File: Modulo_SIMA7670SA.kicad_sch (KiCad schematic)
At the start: 64 parts, among them J1 TBP01R1-508-02BE, J2 DB9 Hembra Impreso 90°, J3 U.FL IPEX1 MALE, J4 SMA-J-P-X-RA-TH1, J5 Jack DC 2.1mm PCB recto, Q1 BSS138, Q2 FDN340P, Q3 FDN340P, Q4 BSS138, Q5 BC327, Q6 2N7000, U1 MAX232, U2 24LC512, U3 BKP-A7670SA (Módulo SIMCOM), U4 MAX706, U5 Black_Pill_STM32F411CEUx, U6 LM2596S_Modulo_Regulable, U7 LM7805_TO220

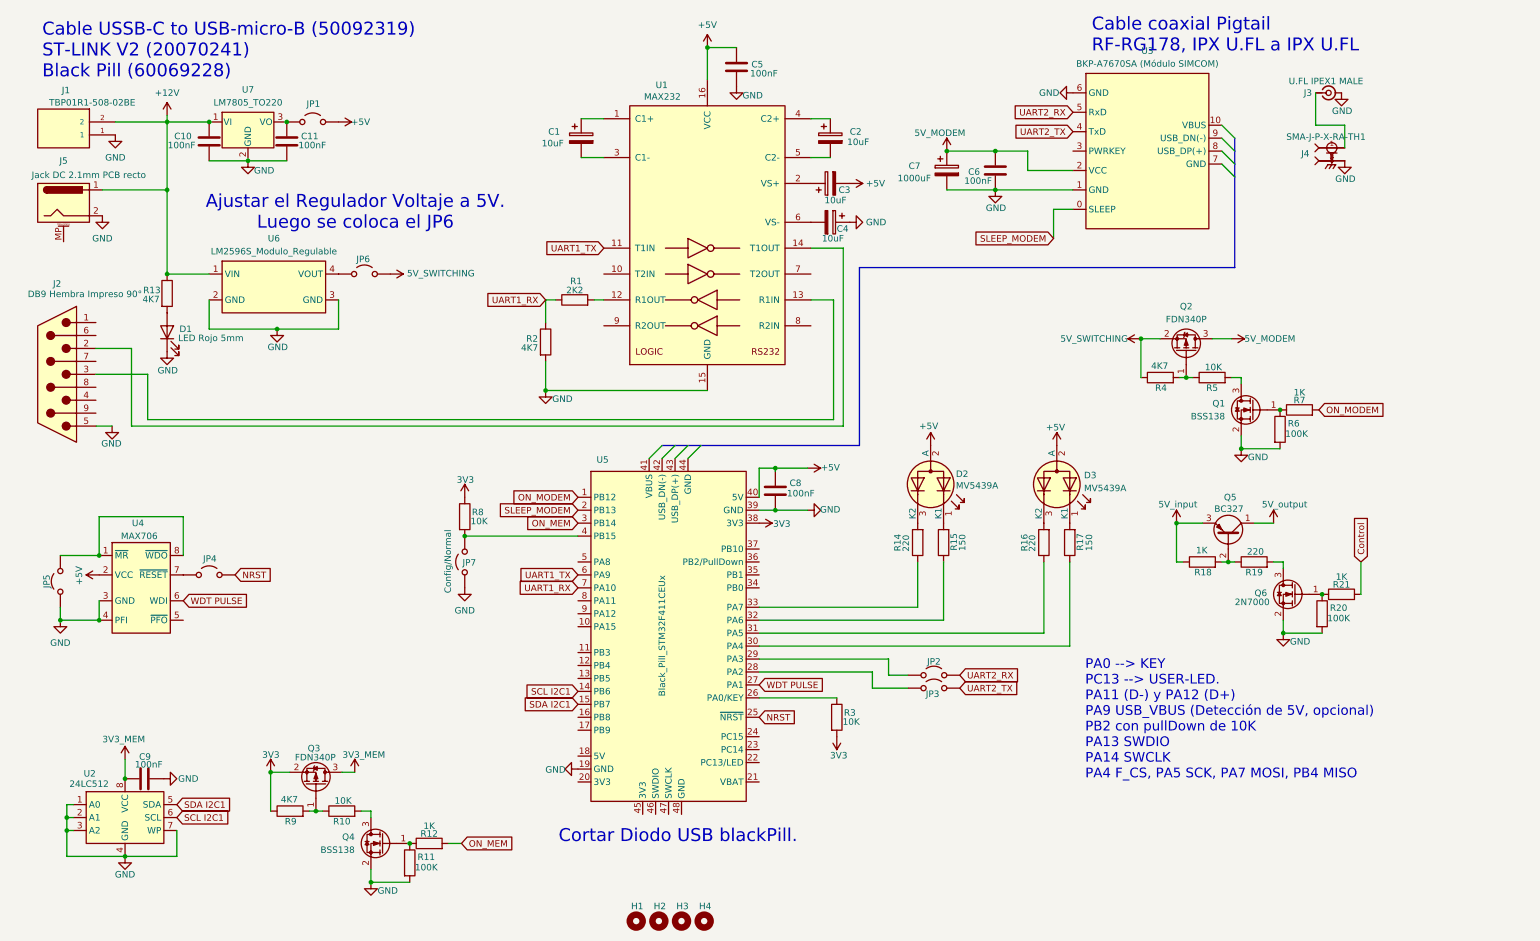
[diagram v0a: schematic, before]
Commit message: Se hicieron modificaciones en los circuitos mosfet para controlar on/off del BKP-A7670SA y de la 24C512.
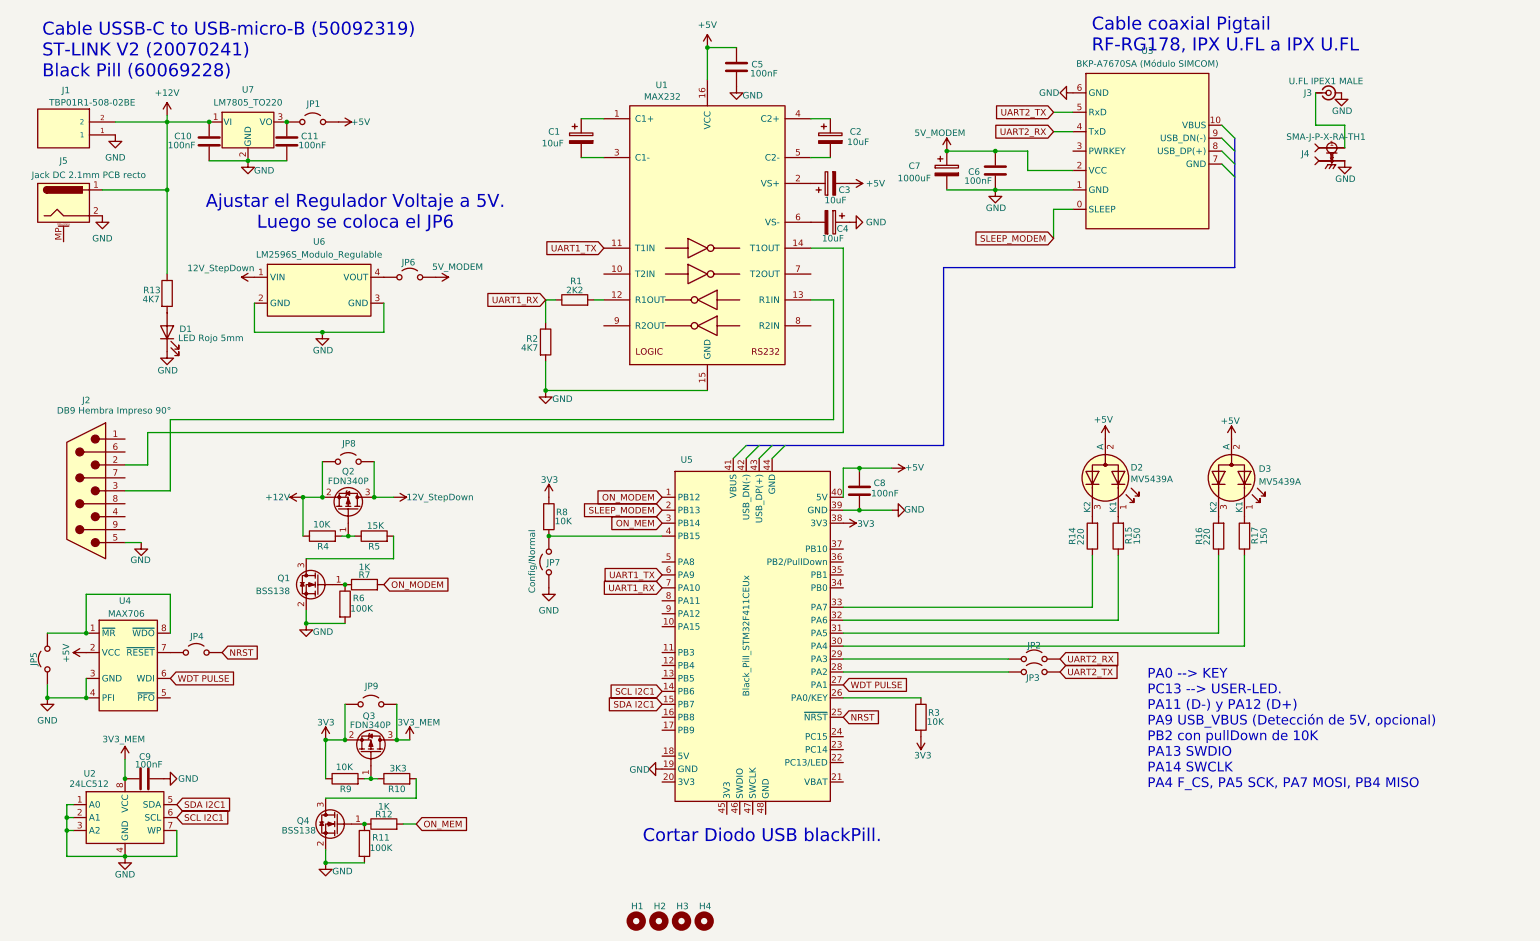
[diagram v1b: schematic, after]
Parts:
- removed Q5: BC327, Package_TO_SOT_THT:TO-92_Inline, symbol Transistor_BJT:BC327
- removed Q6: 2N7000, Package_TO_SOT_SMD:SOT-23, symbol Transistor_FET:BSS138
- removed R18, R21: 1K, Resistor_SMD:R_0805_2012Metric, symbol Device:R
- removed R19: 220, Resistor_SMD:R_0805_2012Metric, symbol Device:R
- removed R20: 100K, Resistor_SMD:R_0805_2012Metric, symbol Device:R
- added JP8, JP9: Jumper_2_Open, Connector_PinHeader_2.54mm:PinHeader_1x02_P2.54mm_Vertical, symbol Jumper:Jumper_2_Open
- R10: value 10K -> 3K3
- R4, R9: value 4K7 -> 10K
- R5: value 10K -> 15K
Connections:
- net +12V: now also Q2.2 (S), R4.1, JP8.1 (A); no longer U6.1 (VIN)
- net 3V3: now also JP9.1 (A)
- net 3V3_MEM: now also JP9.2 (B)
- net 5V_MODEM: now also JP6.2 (B); no longer Q2.3 (D)
- net UART2_RX: now also U3.4 (TxD); no longer U3.5 (RxD)
- net UART2_TX: now also U3.5 (RxD); no longer U3.4 (TxD)
- removed net 5V_SWITCHING: JP6.2 (B), Q2.2 (S), R4.1
- new net 12V_StepDown: JP8.2 (B), Q2.3 (D), U6.1 (VIN)
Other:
- moved on the sheet: C8, D2, D3, J2, JP2, JP3, JP4, JP5, JP6, JP7, Q1, Q2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

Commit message: Estamos haciendo un nuevo PCB porque se hicieron mpodificaciones en el circuito eléctrico para manejar la señal de ON/OFF del BKP-A7670SA en el riel de los 12V.
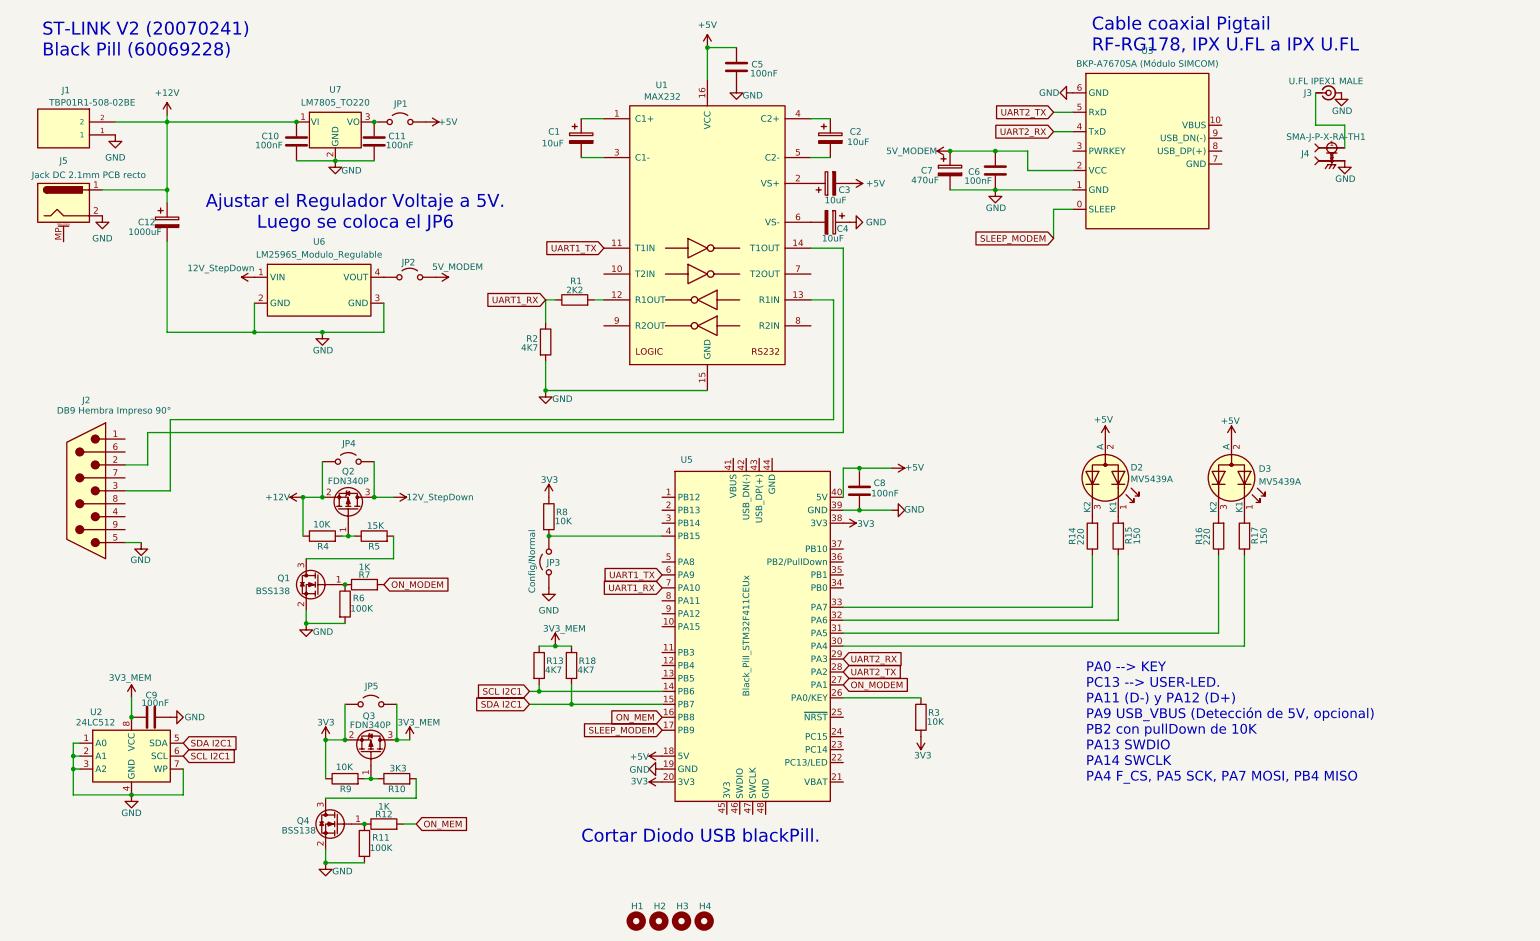
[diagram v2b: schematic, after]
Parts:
- removed D1: LED Rojo 5mm, LED_THT:LED_D5.0mm, symbol Device:LED
- removed JP2, JP3, JP4, JP5: Jumper_2_Open, Connector_PinHeader_2.54mm:PinHeader_1x02_P2.54mm_Vertical, symbol Jumper:Jumper_2_Open
- removed U4: MAX706, Package_SO:SOIC-8_3.9x4.9mm_P1.27mm, symbol New_Library:MAX705
- added C12: 1000uF, Capacitor_THT:CP_Radial_D8.0mm_P5.00mm, symbol Device:C_Polarized
- added R18: 4K7, Resistor_SMD:R_0805_2012Metric, symbol Device:R
- C7: value 1000uF -> 470uF
- renumbered JP6 to JP2, JP7 to JP3, JP8 to JP4, JP9 to JP5
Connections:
- net WDT PULSE is gone; now on net ON_MODEM: U5.27 (PA1)
- net +12V: now also C12.1; no longer R13.1
- net +5V: now also U5.18 (5V)
- net 3V3: now also U5.20 (3V3)
- net 3V3_MEM: now also R13.1, R18.1
- net GND: now also C12.2
- net ON_MEM: now also U5.16 (PB8); no longer U5.3 (PB14)
- net ON_MODEM: no longer U5.1 (PB12)
- net SCL I2C1: now also R13.2
- net SDA I2C1: now also R18.2
- net SLEEP_MODEM: now also U5.17 (PB9); no longer U5.2 (PB13)
- net UART2_RX: now also U5.29 (PA3)
- net UART2_TX: now also U5.28 (PA2)
- net NRST: no longer names the net of U5.25 (~{NRST})
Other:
- note added: "ST-LINK V2 (20070241) Black Pill (60069228)"
- note removed: "Cable USSB-C to USB-micro-B (50092319) ST-LINK V2 (20070241) Black Pill (60069228)"
- moved on the sheet: C10, C11, C9, JP1, U2, U7

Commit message: Adelantando algo del PCB. Fue ncesario modificar GPIOs del STM32 y renombrar rieles de 3.3V; 5V; y GND, para que no tengamos líneas sin rutear.
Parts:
- added C13: 470uF, Capacitor_THT:CP_Radial_D8.0mm_P5.00mm, symbol Device:C_Polarized
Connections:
- net +5V: now also C13.1
- net 3V3: no longer JP5.1 (A), Q3.2 (S), R9.1, U5.20 (3V3)
- net GND: now also C13.2
- new net 3V3_b: JP5.1 (A), Q3.2 (S), R9.1, U5.20 (3V3)
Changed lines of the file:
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@@
 	)
 	(junction
+		(at 186.69 102.87)
+		(diameter 0)
+		(color 0 0 0 0)
+	)
+	(junction
 		(at 119.38 148.59)
 		(diameter 0)
@@
 	)
 	(junction
-		(at 175.895 110.49)
+		(at 114.935 115.57)
 		(diameter 0)
 		(color 0 0 0 0)
 	)
 	(junction
-		(at 114.935 115.57)
+		(at 71.12 179.705)
 		(diameter 0)
 		(color 0 0 0 0)
 	)
 	(junction
-		(at 71.12 179.705)
+		(at 40.005 47.625)
 		(diameter 0)
 		(color 0 0 0 0)
 	)
 	(junction
-		(at 40.005 47.625)
+		(at 175.895 102.87)
 		(diameter 0)
 		(color 0 0 0 0)
@@
 	)
 	(junction
-		(at 175.895 102.235)
+		(at 71.12 155.575)
 		(diameter 0)
 		(color 0 0 0 0)
 	)
 	(junction
-		(at 71.12 155.575)
+		(at 175.895 110.49)
 		(diameter 0)
 		(color 0 0 0 0)
@@
 		(color 0 0 0 0)
 	)
+	(junction
+		(at 186.69 110.49)
+		(diameter 0)
+		(color 0 0 0 0)
+	)
 	(wire
 		(pts
@@
 	(wire
 		(pts
-			(xy 182.245 110.49) (xy 175.895 110.49)
+			(xy 192.405 110.49) (xy 186.69 110.49)
 		)
 		(stroke
@@
 	(wire
 		(pts
-			(xy 175.895 102.235) (xy 182.245 102.235)
+			(xy 175.895 102.87) (xy 186.69 102.87)
 		)
 		(stroke
@@
 	(wire
 		(pts
+			(xy 186.69 110.49) (xy 175.895 110.49)
+		)
+		(stroke
+			(width 0)
+			(type default)
+		)
+	)
+	(wire
+		(pts
 			(xy 113.03 146.05) (xy 137.16 146.05)
 		)
@@
 	(wire
 		(pts
-			(xy 175.895 102.235) (xy 172.72 102.235)
+			(xy 175.895 102.87) (xy 172.72 102.87)
 		)
 		(stroke
@@
 	(wire
 		(pts
+			(xy 186.69 102.87) (xy 192.405 102.87)
+		)
+		(stroke
+			(width 0)
+			(type default)
+		)
+	)
+	(wire
+		(pts
 			(xy 193.675 47.625) (xy 202.565 47.625)
 		)
@@
 	(wire
 		(pts
-			(xy 175.895 102.87) (xy 175.895 102.235)
-		)
-		(stroke
-			(width 0)
-			(type default)
-		)
-	)
-	(wire
-		(pts
 			(xy 208.915 43.815) (xy 208.915 40.005)
 		)
@@
 	(wire
 		(pts
-			(xy 172.72 102.235) (xy 172.72 107.95)
+			(xy 172.72 102.87) (xy 172.72 107.95)
 		)
 		(stroke
@@
 			)
 		)
-		(property "Value" "3V3"
-			(at 69.469 152.146 0)
+		(property "Value" "3V3_b"
+			(at 68.58 152.4 0)
 			(show_name no)
 			(do_not_autoplace no)
@@
 			)
 		)
-		(property "Value" "3V3"
-			(at 132.715 163.703 90)
+		(property "Value" "3V3_b"
+			(at 132.08 163.83 90)
 			(show_name no)
 			(do_not_autoplace no)
@@
 	(symbol
 		(lib_id "power:GND")
-		(at 182.245 110.49 90)
+		(at 192.405 110.49 90)
 		(unit 1)
 		(body_style 1)
@@
 		(dnp no)
 		(property "Reference" "#PWR019"
-			(at 188.595 110.49 0)
+			(at 198.755 110.49 0)
 			(hide yes)
 			(show_name no)
@@
 		)
 		(property "Value" "GND"
-			(at 184.658 110.363 90)
+			(at 194.818 110.363 90)
 			(show_name no)
 			(do_not_autoplace no)
@@
 		)
 		(property "Footprint" ""
-			(at 182.245 110.49 0)
+			(at 192.405 110.49 0)
 			(hide yes)
 			(show_name no)
@@
 		)
 		(property "Datasheet" ""
-			(at 182.245 110.49 0)
+			(at 192.405 110.49 0)
 			(hide yes)
 			(show_name no)
@@
 		)
 		(property "Description" "Power symbol creates a global label with name \"GND\" , ground"
-			(at 182.245 110.49 0)
+			(at 192.405 110.49 0)
 			(hide yes)
 			(show_name no)
@@
 	)
 	(symbol
+		(lib_id "Device:C_Polarized")
+		(at 186.69 106.68 0)
+		(unit 1)
+		(body_style 1)
+		(exclude_from_sim no)
+		(in_bom yes)
+		(on_board yes)
+		(in_pos_files yes)
+		(dnp no)
+		(property "Reference" "C13"
+			(at 189.23 106.68 0)
+			(show_name no)
+			(do_not_autoplace no)
+			(effects
+				(font
+					(size 1.27 1.27)
+				)
+				(justify left)
+			)
+		)
+		(property "Value" "470uF"
+			(at 187.96 108.585 0)
+			(show_name no)
+			(do_not_autoplace no)
+			(effects
+				(font
+					(size 1.27 1.27)
+				)
+				(justify left)
+			)
+		)
+		(property "Footprint" "Capacitor_THT:CP_Radial_D8.0mm_P5.00mm"
+			(at 187.6552 110.49 0)
+			(hide yes)
+			(show_name no)
+			(do_not_autoplace no)
+			(effects
+				(font
+					(size 1.27 1.27)
+				)
+			)
+		)
+		(property "Datasheet" ""
+			(at 186.69 106.68 0)
+			(hide yes)
+			(show_name no)
+			(do_not_autoplace no)
+			(effects
+				(font
+					(size 1.27 1.27)
+				)
+			)
+		)
+		(property "Description" "Polarized capacitor"
+			(at 186.69 106.68 0)
+			(hide yes)
+			(show_name no)
+			(do_not_autoplace no)
+			(effects
+				(font
+					(size 1.27 1.27)
+				)
+			)
+		)
+		(pin "1"
+		)
+		(pin "2"
+		)
+		(instances
+			(project "Modulo_SIMA7670SA"
+				(path "/dcddb0b4-aece-4f57-80c5-ef9bd7fff7ad"
+					(reference "C13")
+					(unit 1)
+				)
+			)
+		)
+	)
+	(symbol
 		(lib_id "Device:R")
 		(at 246.38 115.57 180)
@@
 	(symbol
 		(lib_id "power:+5V")
-		(at 182.245 102.235 270)
+		(at 192.405 102.87 270)
 		(unit 1)
 		(body_style 1)
@@
 		(dnp no)
 		(property "Reference" "#PWR016"
-			(at 178.435 102.235 0)
+			(at 188.595 102.87 0)
 			(hide yes)
 			(show_name no)
@@
 		)
 		(property "Value" "+5V"
-			(at 186.69 102.108 90)
+			(at 196.85 102.743 90)
 			(show_name no)
 			(do_not_autoplace no)
@@
 		)
 		(property "Footprint" ""
-			(at 182.245 102.235 0)
+			(at 192.405 102.87 0)
 			(hide yes)
 			(show_name no)
@@
 		)
 		(property "Datasheet" ""
-			(at 182.245 102.235 0)
+			(at 192.405 102.87 0)
 			(hide yes)
 			(show_name no)
@@
 		)
 		(property "Description" "Power symbol creates a global label with name \"+5V\""
-			(at 182.245 102.235 0)
+			(at 192.405 102.87 0)
 			(hide yes)
 			(show_name no)

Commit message: Ya está todo ruteado, falta una sola net sin rutear que no se cual es. Solo hay que revisar.
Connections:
- net +5V: no longer C3.2, C5.1, U1.16 (VCC), U5.18 (5V)
- net GND: now also J2.0
- new net +5V_b: C3.2, C5.1, U1.16 (VCC), U5.18 (5V)
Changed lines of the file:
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@@
 	)
 	(junction
+		(at 31.75 116.84)
+		(diameter 0)
+		(color 0 0 0 0)
+	)
+	(junction
 		(at 202.565 40.005)
 		(diameter 0)
@@
 	(wire
 		(pts
+			(xy 31.75 120.65) (xy 31.75 116.84)
+		)
+		(stroke
+			(width 0)
+			(type default)
+		)
+	)
+	(wire
+		(pts
 			(xy 36.195 101.6) (xy 36.195 95.25)
 		)
@@
 	(wire
 		(pts
+			(xy 22.86 120.65) (xy 31.75 120.65)
+		)
+		(stroke
+			(width 0)
+			(type default)
+		)
+	)
+	(wire
+		(pts
 			(xy 85.09 148.59) (xy 85.09 155.575)
 		)
@@
 		(pin "6"
 		)
+		(pin "0"
+		)
 		(instances
 			(project "Modulo_SIMA7670SA"
@@
 		(in_pos_files yes)
 		(dnp no)
-		(fields_autoplaced yes)
 		(property "Reference" "#PWR04"
 			(at 170.18 46.355 0)
@@
 			)
 		)
-		(property "Value" "+5V"
-			(at 177.165 46.3549 90)
+		(property "Value" "+5V_b"
+			(at 177.165 46.355 90)
 			(show_name no)
 			(do_not_autoplace no)
@@
 		(in_pos_files yes)
 		(dnp no)
-		(fields_autoplaced yes)
 		(property "Reference" "#PWR05"
 			(at 146.05 23.495 0)
@@
 			)
 		)
-		(property "Value" "+5V"
-			(at 146.05 15.24 0)
+		(property "Value" "+5V_b"
+			(at 142.875 16.51 0)
 			(show_name no)
 			(do_not_autoplace no)
@@
 					(size 1.27 1.27)
 				)
+				(justify left)
 			)
 		)
@@
 			)
 		)
-		(property "Value" "+5V"
-			(at 132.715 158.877 90)
+		(property "Value" "+5V_b"
+			(at 131.445 158.75 90)
 			(show_name no)
 			(do_not_autoplace no)
